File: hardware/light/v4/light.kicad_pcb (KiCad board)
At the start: 2 copper layers, 30 x 30 mm, 21 parts, among them J1 PH2-16-UA, J2 Conn_01x09, J3 Conn_01x09, J4 B3B-XH-A, Q1 DMG2301L, Q2 MMBT3904, U1 LP2985-50DBVR, U2 SN74LVC1G17DBVR

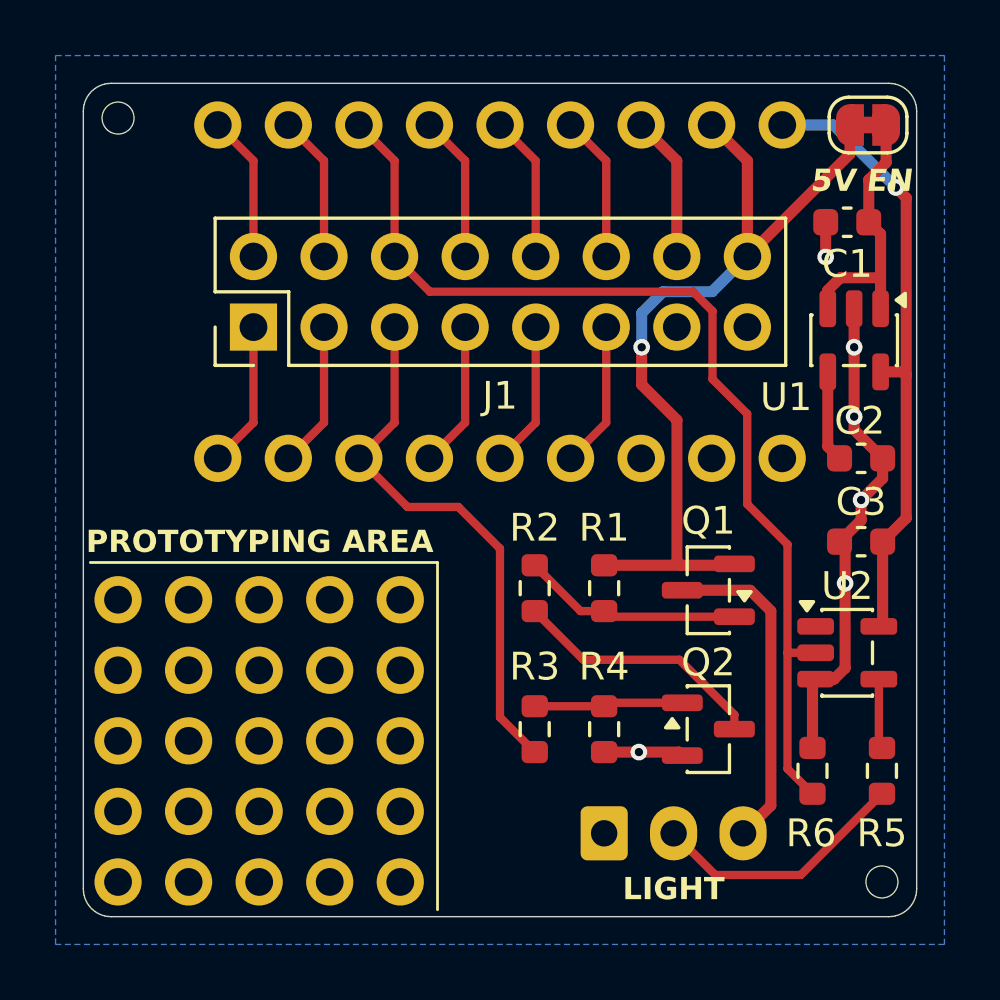
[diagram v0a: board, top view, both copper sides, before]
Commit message: First draft of Minuet light accessory v4.
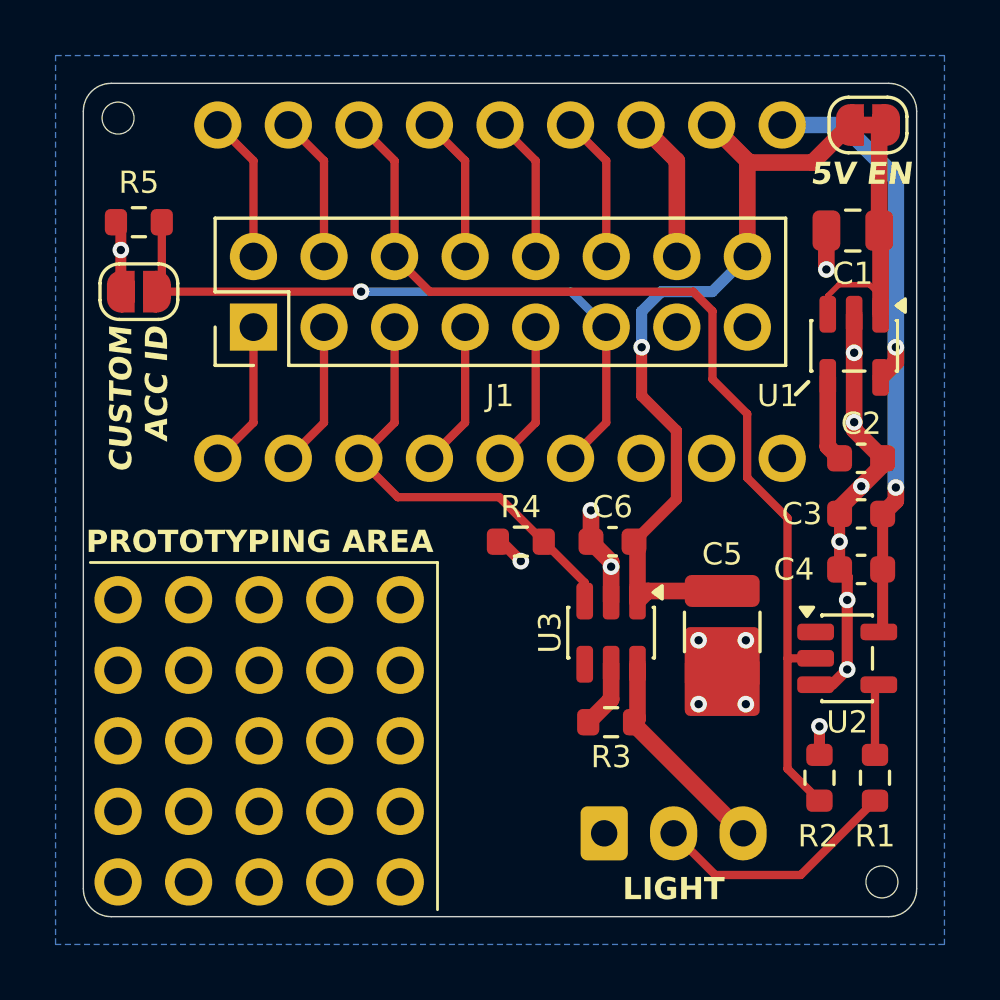
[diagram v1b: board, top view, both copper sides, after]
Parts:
- removed Q1: DMG2301L, Package_TO_SOT_SMD:SOT-23
- removed Q2: MMBT3904, Package_TO_SOT_SMD:SOT-23
- removed the R1 at (118.8, 118.2)
- removed the R2 at (116.2, 118.2)
- added C4: 100n, Capacitor_SMD:C_0603_1608Metric, F.Cu at (128.0, 117.5)
- added C5: 10u, Capacitor_SMD:C_1210_3225Metric, F.Cu at (123.0, 119.8)
- added C6: 100n, Capacitor_SMD:C_0603_1608Metric, F.Cu at (119.0, 116.5)
- added JP2: SolderJumper_2_Open, Jumper:SolderJumper-2_P1.3mm_Open_RoundedPad1.0x1.5mm, F.Cu at (102.0, 107.5)
- added R5: 100K, Resistor_SMD:R_0603_1608Metric, F.Cu at (102.0, 105.0)
- added U3: TPS22810(-Q1), Package_TO_SOT_SMD:SOT-23-6, F.Cu at (119.0, 119.8)
- C1: footprint Capacitor_SMD:C_0603_1608Metric -> Capacitor_SMD:C_0805_2012Metric
- R3: value 10K -> 1K
- moved R4 7.39 mm to (115.8, 116.5), turned to 0 degrees
- moved R3 2.76 mm to (119.0, 123.0), turned to 180 degrees
- moved C3 1.00 mm to (128.0, 115.5)
- moved C1 0.36 mm to (127.7, 105.3)
- moved R1 0.35 mm to (128.5, 125.0)
- moved R2 0.35 mm to (126.5, 125.0)
- moved U1 0.20 mm to (127.8, 109.5)
- moved U2 0.20 mm to (127.5, 120.7)
- renumbered J4 to J2, J2 to J3, J3 to J4, R5 to R1, R6 to R2
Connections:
- net GPIO5 renamed GPIO14
- net RESERVED renamed ACC_ID
- net SCL renamed I2C_SCL
- net SDA renamed I2C_SDA
- J1 pad 5: GPIO6 -> GPIO15
- J3 pad 3: GPIO6 -> GPIO15
- R3 pad 1: Net-(Q2-B) -> /LOAD
- R3 pad 2: GPIO6 -> Net-(U3-QOD)
- R4 pad 2: Net-(Q2-B) -> GPIO15
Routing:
- net GPIO6: track 19.5 -> 0.00 mm
- net ACC_ID: track 5.26 -> 24.3 mm, vias 0 -> 1
- net GPIO15: track 0.00 -> 15.9 mm
- net Net-(Q2-C): track 9.25 -> 0.00 mm
- net Net-(Q1-G): track 7.67 -> 0.00 mm
- net Net-(Q2-B): track 5.19 -> 0.00 mm
- net /LOAD: track 11.9 -> 7.69 mm
- net Net-(U3-QOD): track 0.00 -> 2.43 mm
- net GND: track 21.7 -> 24.0 mm, vias 6 -> 16
- net +12V: track 30.3 -> 28.8 mm
- net Net-(JP1-A): track 9.80 -> 10.4 mm
- net +5V: track 22.4 -> 22.8 mm, vias 1 -> 2
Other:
- board text added: "5V 12V 3V3 LCK TX SDA G14 G0 RST"
- board text added: "CUSTOM ACC ID"
- board text added: "GND GND GND ID RX SCL G15 G1 BT"
- board text removed: "5V 12V 3V3 LCK TX SDA GP5 GP0 RST"
- board text removed: "GND GND GND NC RX SCL GP6 GP1 BT"

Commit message: Add DNP footprint for CT slew rate capacitor.
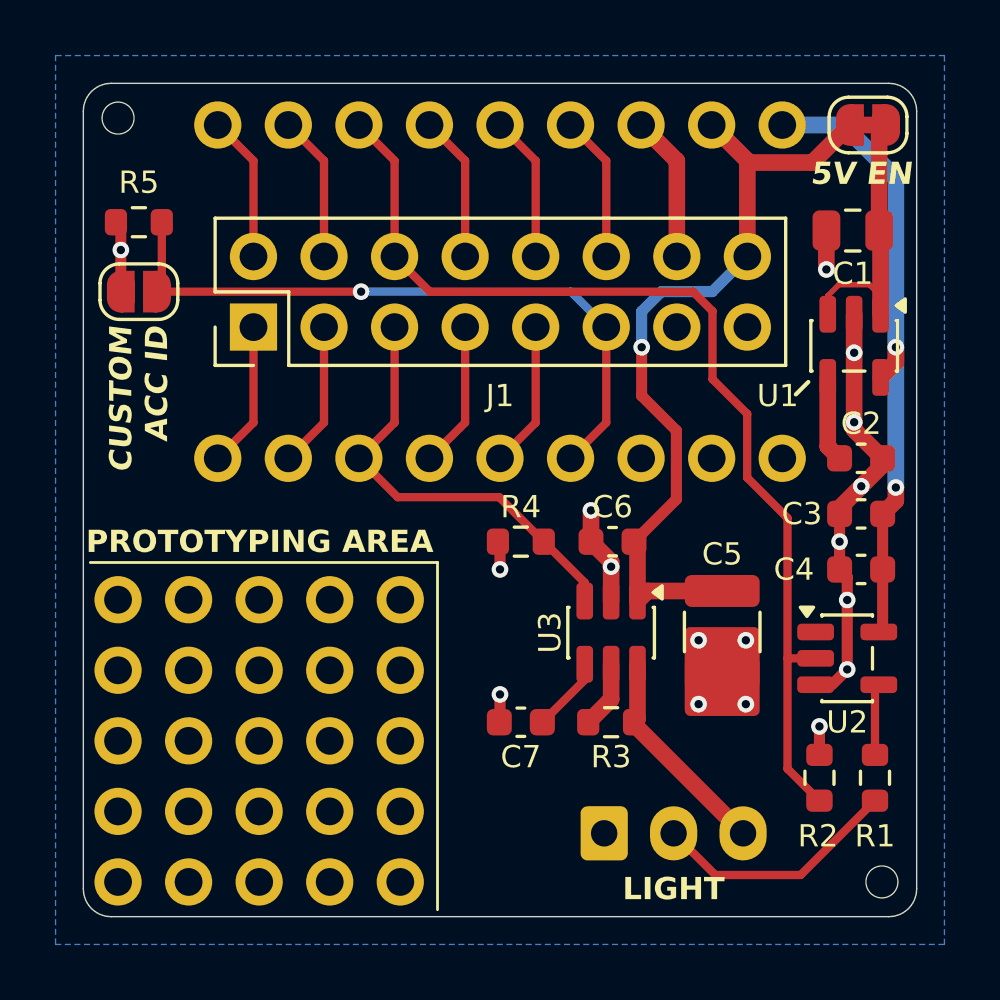
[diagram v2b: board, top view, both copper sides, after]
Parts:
- added C7: 10n, Capacitor_SMD:C_0603_1608Metric, F.Cu at (115.8, 123.0)
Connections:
- U3 pad 4: unconnected-(U3-CT-Pad4) -> Net-(U3-CT)
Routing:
- net Net-(U3-CT): track 0.00 -> 2.72 mm
- net GND: track 24.0 -> 25.0 mm, vias 16 -> 17

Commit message: Prepare light accessory for fabrication
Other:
- board text added: "5V 12V 3V3 LCK TXD SDA G14 G0 RST"
- board text added: "GND GND GND ID RXD SCL G15 G1 BT"
- board text removed: "5V 12V 3V3 LCK TX SDA G14 G0 RST"
- board text removed: "GND GND GND ID RX SCL G15 G1 BT"
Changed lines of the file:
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@@
 		)
 	)
-	(gr_text "GND\n\nGND\n\nGND\n\nID\n\nRX\n\nSCL\n\nG15\n\nG1\n\nBT"
+	(gr_text "GND\n\nGND\n\nGND\n\nID\n\nRXD\n\nSCL\n\nG15\n\nG1\n\nBT"
 		(locked yes)
 		(at 115 112.25 270)
@@
 		)
 	)
-	(gr_text "5V\n\n12V\n\n3V3\n\nLCK\n\nTX\n\nSDA\n\nG14\n\nG0\n\nRST"
+	(gr_text "5V\n\n12V\n\n3V3\n\nLCK\n\nTXD\n\nSDA\n\nG14\n\nG0\n\nRST"
 		(locked yes)
 		(at 115 102.75 270)
@@
 		(hatch edge 0.5)
 		(connect_pads
-			(clearance 0.5)
+			(clearance 0.3)
 		)
 		(min_thickness 0.25)
